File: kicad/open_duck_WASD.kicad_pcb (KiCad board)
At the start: 2 copper layers, 275 x 163 mm, 20 parts

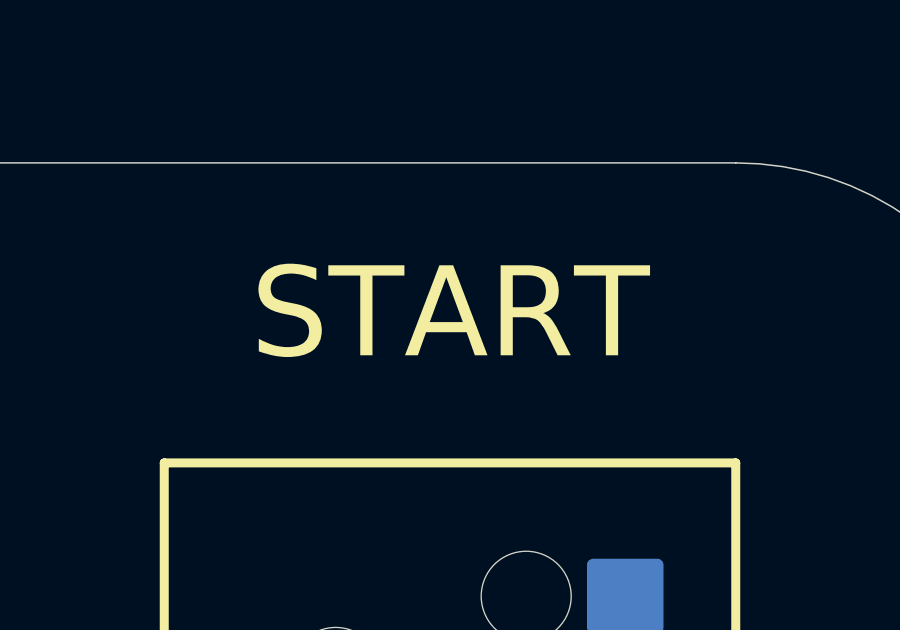
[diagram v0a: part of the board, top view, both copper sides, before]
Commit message: Update label on turbo
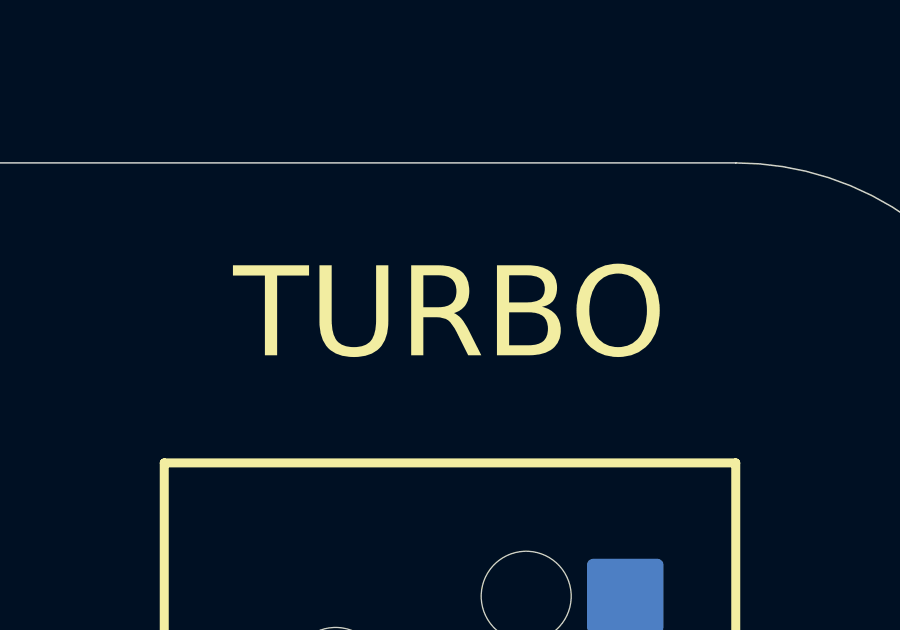
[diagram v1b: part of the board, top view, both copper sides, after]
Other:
- board text added: "TURBO"
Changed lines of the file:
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@@
 		)
 		(group ""
-			(members "093a571f-ad4d-4690-b527-29e0d0fe9c1d" "107da40b-b185-43a5-aa01-ad807b7a2e3f"
-				"1423f7a8-5273-4517-9bbf-017e99224829" "15b93fc3-5356-4c7c-a64f-878bde9fc0d5"
-				"1663912e-672b-4bda-9524-4b23df706d63" "24d3248f-f500-4265-8374-814328092401"
-				"251e71af-a8d5-400f-b6b4-82e58d432c19" "26c63ba5-cc1c-4222-ac0f-c41b95e9daa5"
-				"27383131-3ddc-47a5-b287-7cfd495109c5" "2d8ef580-eb05-4697-b4f6-5827e81c414a"
-				"2db84326-e316-45a1-8c3c-8ad51076f653" "313d8b72-37da-4269-ae5e-2d58ff986af2"
-				"36689134-431b-4639-ba5b-6c3efc0dfd82" "37fd0545-99bd-4911-a175-3b69a7fea636"
-				"3bf414d4-21ca-4743-ac26-6582f4a498ec" "3f8ba0d4-e61b-48b6-9a90-d2ac5ec97bb3"
-				"403c39ec-a627-4912-ad66-fdcd8494f141" "41eccf0a-9090-4d89-b2d1-6f4a4fc909bc"
-				"45e08719-38c1-49de-8883-ed0ea6d0f71d" "4c438b68-e804-4aa5-998c-ed9bcea96183"
-				"5413616c-aaaf-4323-a6d6-bf06c7165f65" "5ceb216b-e8d3-45f6-9ad0-24f7e5f78aab"
-				"5d6cb401-e5f3-41ef-9f75-2cf9a5bcdca2" "5f09f7fc-fe72-462f-8e1b-d5e9a488353e"
-				"635b9275-1d50-4c88-b490-7b7e49af2491" "71646c7f-96ef-48a8-8827-fee8c632009e"
-				"7317a3ff-f992-4a12-9636-2b8fe2d6ab75" "7356d62e-fd58-4162-9de3-17990b862605"
-				"8a1e2985-3547-4fef-90e9-fd3369ec6bf5" "955c67a4-268b-4621-a9a2-76f19ba22415"
-				"960840f9-bd52-409b-8455-7c0f155165b0" "9993149c-a564-4aef-923a-a5f302c3e0c9"
-				"a290cbe6-3b6a-4614-9c46-6dab81d313a8" "aa0fb0f2-3c6f-4da7-bb9e-d93fa852f763"
-				"aa9482b3-53ff-401b-a83c-68ddc717dcdc" "abdffcfd-989b-44dd-a430-7d7d1f57db41"
-				"ac630b8f-69ee-449b-baa8-f2218f35ba3e" "b5c4677f-def7-46fa-a115-aa12a5173185"
-				"bace4414-a9b4-474c-9719-641e9e679879" "c164a312-7760-4f9c-b4c4-580aef1e5f5b"
-				"c4f2b195-64f0-4a12-a8ed-c5c97a7ddbcd" "c9020456-f6e6-4865-9bf6-6db49731b596"
-				"d49aef96-0b0a-4bcd-bebd-d5038e6c5da6" "f1915481-1613-4b18-86c2-d1c1f6f1f216"
-				"f1e35c0e-0f32-4911-9f7a-811be8ba792b" "f980a12f-41b4-493c-bd88-685eeb6169f6"
-				"fbb181ca-6891-45c2-9e96-318ef8c5aa4c" "fe4cf39c-25c7-47f5-adaf-08c7a8dcf016"
-			)
-		)
-		(group ""
-			(members "0c75b276-904c-47fe-9d2d-1509e03b387b" "2904c4b0-45b6-4607-99f7-e1e8610258dd"
-				"2977d173-5807-4b39-b894-cd1380405db8" "2cb37ffa-1ba2-43fa-aec9-456e8c716bc3"
-				"3d4a08dc-cb8d-4c3c-bcbb-c46d9b87cdbd" "476a3802-4368-4db0-88be-1d4642f4c9c0"
-				"5520f20e-4025-497a-b13f-e6d9c22b32fa" "562494ed-72e7-4fee-ae4d-92a65e54bf1f"
-				"56509297-4259-4436-b527-73123570015a" "58a7f528-8a9a-4b4f-a0a4-6569ce073915"
-				"5df23df0-f82f-48b8-b896-d1327366be90" "699062b3-3328-4460-98c4-fe3c0520f6d5"
-				"73befebf-01ef-4744-9144-f6c7892fd047" "746d2f83-bd0a-48dd-afbe-3a4db0588229"
-				"989f84b9-03dc-43c5-b3af-2f6de1d08b93" "9ce5442c-a819-4ca6-8408-2501074f9426"
-				"a965412e-64b7-4b4c-9f4f-b6c2fe69cedb" "ad53afe6-8209-49de-ad80-cb6449e3a979"
-				"b8d8f741-6301-41c4-873a-59be288bd3f0" "cb5ab8b9-2f16-40db-8748-9db41e432c9e"
-				"d72c9cc2-773e-48ca-84d8-8c42f7f405e5" "db9cb9d3-9f17-439b-8352-4741f551f5c9"
-				"dffe6e58-28ff-4534-ba0c-66a3738894f8" "eae6a83d-3e45-4002-935b-8e0367fe1687"
-				"eec59147-a348-469d-bf4b-5e2f50a5ad7c" "f0a411ca-d4cf-4380-978e-72397db9be42"
-				"f2c33254-a395-456d-993f-fdcb86c024bf" "f33b488f-b21f-4533-89bf-44413796e327"
-			)
-		)
-		(group ""
 			(members "032aab77-3571-4ab2-9b80-b73d3dd3374f" "0cd9a332-c941-47bf-8fd2-03a7741391ce"
 				"107da40b-b185-43a5-aa01-ad807b7a2e3f" "1423f7a8-5273-4517-9bbf-017e99224829"
@@
 		)
 		(group ""
+			(members "0c75b276-904c-47fe-9d2d-1509e03b387b" "2904c4b0-45b6-4607-99f7-e1e8610258dd"
+				"2977d173-5807-4b39-b894-cd1380405db8" "2cb37ffa-1ba2-43fa-aec9-456e8c716bc3"
+				"3d4a08dc-cb8d-4c3c-bcbb-c46d9b87cdbd" "476a3802-4368-4db0-88be-1d4642f4c9c0"
+				"5520f20e-4025-497a-b13f-e6d9c22b32fa" "562494ed-72e7-4fee-ae4d-92a65e54bf1f"
+				"56509297-4259-4436-b527-73123570015a" "58a7f528-8a9a-4b4f-a0a4-6569ce073915"
+				"5df23df0-f82f-48b8-b896-d1327366be90" "699062b3-3328-4460-98c4-fe3c0520f6d5"
+				"73befebf-01ef-4744-9144-f6c7892fd047" "746d2f83-bd0a-48dd-afbe-3a4db0588229"
+				"989f84b9-03dc-43c5-b3af-2f6de1d08b93" "9ce5442c-a819-4ca6-8408-2501074f9426"
+				"a965412e-64b7-4b4c-9f4f-b6c2fe69cedb" "ad53afe6-8209-49de-ad80-cb6449e3a979"
+				"b8d8f741-6301-41c4-873a-59be288bd3f0" "cb5ab8b9-2f16-40db-8748-9db41e432c9e"
+				"d72c9cc2-773e-48ca-84d8-8c42f7f405e5" "db9cb9d3-9f17-439b-8352-4741f551f5c9"
+				"dffe6e58-28ff-4534-ba0c-66a3738894f8" "eae6a83d-3e45-4002-935b-8e0367fe1687"
+				"eec59147-a348-469d-bf4b-5e2f50a5ad7c" "f0a411ca-d4cf-4380-978e-72397db9be42"
+				"f2c33254-a395-456d-993f-fdcb86c024bf" "f33b488f-b21f-4533-89bf-44413796e327"
+			)
+		)
+		(group ""
 			(members "156e1606-9167-4aa4-9c21-de4bdbed5c59" "197c99ff-26f8-4fbc-83f3-33a7edcbc44b"
 				"3eb44e43-79ff-490c-98f4-25c8bf8b173c" "450d544b-ddcd-46f5-8f33-efcfb30f7a2f"
@@
 		)
 		(group ""
+			(members "093a571f-ad4d-4690-b527-29e0d0fe9c1d" "27383131-3ddc-47a5-b287-7cfd495109c5"
+				"3bf414d4-21ca-4743-ac26-6582f4a498ec" "45e08719-38c1-49de-8883-ed0ea6d0f71d"
+				"5d6cb401-e5f3-41ef-9f75-2cf9a5bcdca2" "955c67a4-268b-4621-a9a2-76f19ba22415"
+				"c9020456-f6e6-4865-9bf6-6db49731b596" "f1915481-1613-4b18-86c2-d1c1f6f1f216"
+			)
+		)
+		(group ""
 			(members "ba424da7-da89-4e90-bae7-91aeb1cb0a79" "ec13bd04-187d-4d99-b339-ea034f1b0511")
 		)
@@
 		)
 	)
-	(gr_text "START\n"
+	(gr_text "TURBO"
 		(at 266.475 19.875 0)
 		(layer "F.SilkS")

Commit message: fix spelling
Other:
- board text added: "UP"
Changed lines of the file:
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@@
 		)
 	)
-	(gr_text "BACK\n"
+	(gr_text "UP"
 		(at 113.6386 71.625 325)
 		(layer "F.SilkS")
